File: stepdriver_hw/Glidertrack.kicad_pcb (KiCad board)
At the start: 2 copper layers, 25 parts

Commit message: HW: start to trace pcb.
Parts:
- added C15: C, CAP_0603, F.Cu at (261.6, 186.7)
- added C16: C, CAP_0603, F.Cu at (256.5, 186.7)
- added C17: C, CAP_0603, F.Cu at (265.4, 186.7)
- added D1: DIODE, DIODE_SOD323, F.Cu at (172.7, 144.8)
- added D2: LED, LED_ANGLE, F.Cu at (226.1, 186.7)
- added D3: LED, LED_ANGLE, F.Cu at (231.1, 186.7)
- added D4: LED, LED_ANGLE, F.Cu at (234.9, 186.7)
- added DA3: LD1117, SOT223, F.Cu at (154.9, 151.1)
- added F1: FUSE0R, RES_0603, F.Cu at (243.8, 186.7)
- added R6: R, RES_0603, F.Cu at (247.7, 186.7)
- added R7: R, RES_0603, F.Cu at (238.8, 186.7)
- added R8: R, RES_0603, F.Cu at (234.9, 195.6)
- added XL10: CONN_8, CONN_PLS-8, F.Cu at (152.4, 174.0)
- added XL3: CONN_3, CONN_PLS-3, F.Cu at (204.5, 170.2)
- added XL4: CONN_2, CONN_PLS-2, F.Cu at (204.5, 162.6)
- added XL5: CONN_3, CONN_PLS-3, F.Cu at (146.1, 166.4)
- added XL6: CONN_10, CONN_IDC_2X5, F.Cu at (138.4, 149.9)
- added XL7: CONN_3, CONN_PLS-3, F.Cu at (135.9, 168.9)
- added XL8: BARREL_SOCKET, CONN_BARREL, F.Cu at (152.4, 142.2)
- added XL9: CONN_8, CONN_PLS-8, F.Cu at (174.0, 174.0)
- added XTAL1: CRYSTAL, CRYSTAL_HC49, F.Cu at (181.6, 162.6)
- moved C5 290.5 mm to (265.4, 191.8)
- moved R4 288.7 mm to (256.5, 191.8)
- moved C6 284.9 mm to (261.6, 191.8)
- moved C11 279.1 mm to (234.9, 191.8)
- moved R1 274.9 mm to (252.7, 186.7)
- moved C8 273.0 mm to (252.7, 191.8)
- moved C12 272.6 mm to (229.9, 191.8)
- moved C1 272.2 mm to (226.1, 195.6)
- moved C10 267.1 mm to (226.1, 191.8)
- moved C9 266.6 mm to (247.7, 191.8)
- moved C2 265.9 mm to (221.0, 195.6)
- moved R2 265.2 mm to (229.9, 195.6)
- moved C14 261.4 mm to (243.8, 191.8)
- moved C3 260.8 mm to (217.2, 195.6)
- moved R3 258.4 mm to (221.0, 191.8)
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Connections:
- DA1 pad 4: +3.3V -> +5V
- DA1 pad 5: +5V -> +3.3V
- DD1 pad 10: (no net) -> /ENDSTOP1
- DD1 pad 11: (no net) -> /ENDSTOP2
- DD1 pad 12: (no net) -> /WIFI_TX
- DD1 pad 13: (no net) -> /WIFI_RX
- DD1 pad 14: (no net) -> /MOTOR_SPI_CS
- DD1 pad 15: (no net) -> /MOTOR_SPI_SCK
- DD1 pad 16: (no net) -> /MOTOR_SPI_MISO
- DD1 pad 17: (no net) -> /MOTOR_SPI_MOSI
- DD1 pad 18: (no net) -> /MOTOR_STBY
- DD1 pad 19: (no net) -> /MOTOR_BUSY
- DD1 pad 20: (no net) -> /MOTOR_FLAG
- DD1 pad 21: (no net) -> /GPIOB10
- DD1 pad 22: (no net) -> /GPIOB11
- DD1 pad 25: (no net) -> /GPIOB12
- DD1 pad 26: (no net) -> /GPIOB13
- DD1 pad 27: (no net) -> /GPIOB14
- DD1 pad 28: (no net) -> /GPIOB15
- DD1 pad 29: (no net) -> /MOTOR_STCK
- DD1 pad 30: (no net) -> /DEBUG_TX
- DD1 pad 31: (no net) -> /DEBUG_RX
- DD1 pad 39: (no net) -> /GPIOB3
- DD1 pad 40: (no net) -> /GPIOB4
- DD1 pad 41: (no net) -> /GPIOB5
- DD1 pad 42: (no net) -> /GPIOB6
- DD1 pad 43: (no net) -> /GPIOB7
- DD1 pad 45: (no net) -> /GPIOB8
- DD1 pad 46: (no net) -> /GPIOB9
- MDL1 pad 14: (no net) -> N-0000074
- MDL1 pad 15: (no net) -> N-0000075
- MDL1 pad 2: (no net) -> /WIFI_BOOT
- MDL1 pad 23: (no net) -> GND
- MDL1 pad 24: (no net) -> +3.3V
- MDL1 pad 3: (no net) -> /WIFI_RESET
- MDL1 pad 5: (no net) -> N-0000076
- MDL1 pad 6: (no net) -> /WIFI_RX
- MDL1 pad 8: (no net) -> /WIFI_TX
- MDL1 pad PAD: (no net) -> GND
- XL1 pad 1: +5V -> N-0000069
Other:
- board outline added: 73.7 x 44.4 mm

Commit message: HW: component placed.
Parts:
- removed D2, D3, D4: LED, LED_ANGLE
- removed XL10: CONN_8, CONN_PLS-8
- added C18: 0.1u, CAP_0603, F.Cu at (144.2, 151.7)
- added DA4: EEPROM_SPI, SO8E, F.Cu at (162.6, 156.6)
- added LINK_UP1: LED, LED_ANGLE, F.Cu at (116.8, 153.4)
- added POWER_UP1: LED, LED_ANGLE, F.Cu at (116.8, 157.6)
- added R10: 22K, RES_0603, F.Cu at (147.6, 135.9)
- added R9: 22K, RES_0603, F.Cu at (147.6, 134.3)
- added RUN1: LED, LED_ANGLE, F.Cu at (116.8, 161.8)
- C10, C9: value C -> 15p
- C15: value C -> 0.1u
- C16: value C -> 10u
- R5: value R -> 1K2
- R6, R7, R8: value R -> 22R
- XTAL1: value CRYSTAL -> 8/16 MHz
- moved R6 132.1 mm to (118.8, 157.6), turned to 90 degrees
- moved R7 124.4 mm to (118.8, 153.4), turned to 90 degrees
- moved R8 121.0 mm to (118.8, 161.8), turned to 90 degrees
- moved C9 115.2 mm to (137.9, 156.4), turned to 270 degrees
- moved R4 109.6 mm to (159.0, 141.8), turned to 90 degrees
- moved C13 101.9 mm to (147.2, 147.1), turned to 90 degrees
- moved C17 101.4 mm to (169.0, 155.2)
- moved F1 99.5 mm to (147.9, 160.2), turned to 180 degrees
- moved C5 99.3 mm to (171.8, 158.7), turned to 90 degrees
- moved C14 97.4 mm to (157.7, 146.4), turned to 90 degrees
- moved C6 97.3 mm to (170.2, 158.7), turned to 90 degrees
- moved R1 96.7 mm to (166.2, 143.5), turned to 270 degrees
- moved C15 96.6 mm to (174.9, 144.1), turned to 180 degrees
- moved C10 93.8 mm to (137.9, 159.7), turned to 90 degrees
- moved C8 92.0 mm to (169.0, 153.6)
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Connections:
- DD1 pad 21: /GPIOB10 -> /EE_WRITE
- DD1 pad 22: /GPIOB11 -> /EE_HOLD
- DD1 pad 25: /GPIOB12 -> (no net)
- DD1 pad 26: /GPIOB13 -> /EE_SCK
- DD1 pad 27: /GPIOB14 -> /EE_MISO
- DD1 pad 28: /GPIOB15 -> /EE_MOSI
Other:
- board size 73.7 x 44.4 mm -> 73.2 x 38.4 mm

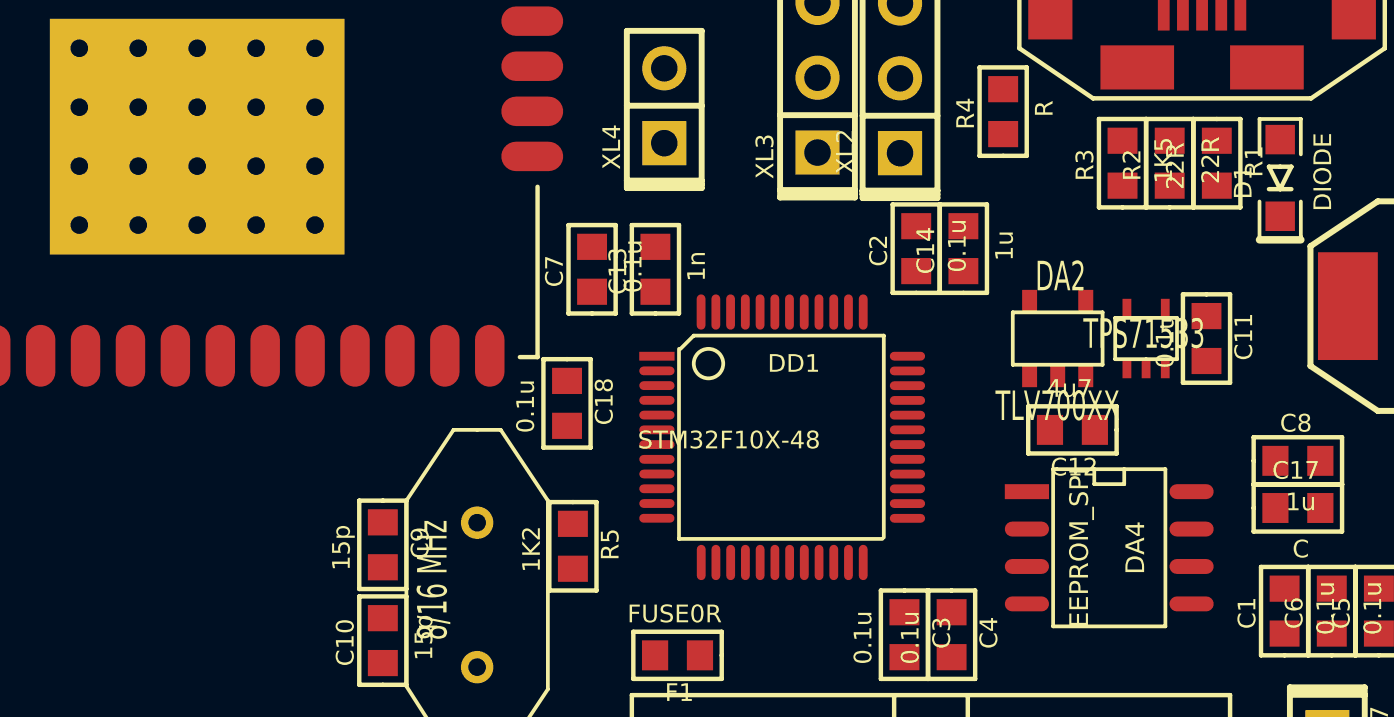
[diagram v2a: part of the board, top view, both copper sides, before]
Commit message: HW: added MOSFET transistor on power WiFi module.
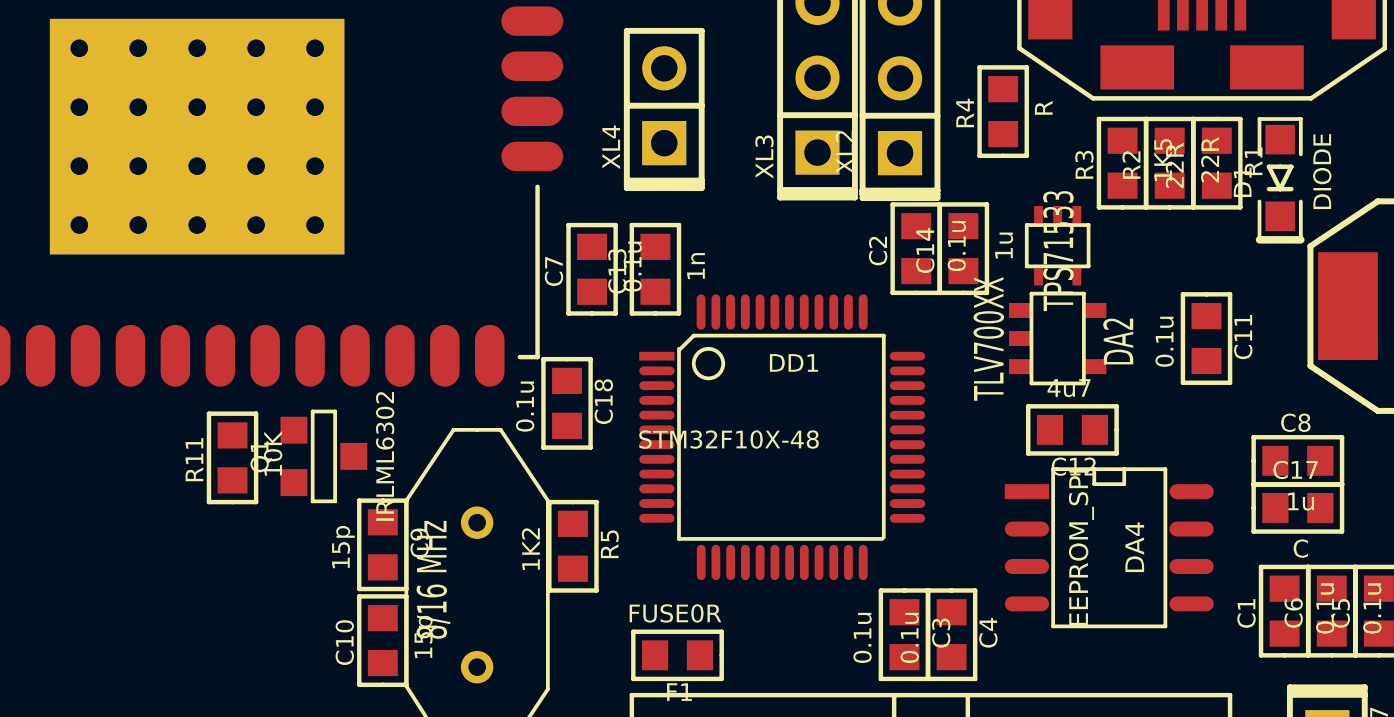
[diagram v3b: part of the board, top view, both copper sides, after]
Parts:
- added Q1: IRLML6302, SOT23, F.Cu at (135.9, 153.4)
- added R11: 10K, RES_0603, F.Cu at (132.8, 153.5)
- moved DA1 4.35 mm to (160.8, 146.3), turned to 270 degrees
- turned DA2 to 270 degrees
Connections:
- C17 pad 1: +3.3V -> N-0000083
- MDL1 pad 24: +3.3V -> N-0000083
- R10 pad 1: +3.3V -> N-0000083
- R9 pad 1: +3.3V -> N-0000083
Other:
- net class Default: clearance 0.254 -> 0.2; trace_width 0.254 -> 0.2; via_dia 0.889 -> 0.8; via_drill 0.635 -> 0.4
- net class PWR added: clearance 0.3, trace_width 0.5, via_dia 0.8, via_drill 0.4
- rule pad_to_mask_clearance: 0 -> 0.2
- rule trace_clearance: 0.254 -> 0.2
- rule trace_min: 0.254 -> 0.2
- rule via_min_drill: 0.508 -> 0.3
- rule via_min_size: 0.889 -> 0.7

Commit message: HW: PCB design proceed.
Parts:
- added HOLE1: HOLE_METALLED, Hole3_5_out6mm, F.Cu at (319.2, 93.8)
- added HOLE2: HOLE_METALLED, Hole3_5_out6mm, F.Cu at (274.0, 100.9)
- moved XL9 169.2 mm to (279.0, 78.7)
- moved R4 163.7 mm to (310.5, 79.7), turned to 0 degrees
- moved RUN1 163.0 mm to (257.1, 78.9), turned to 180 degrees
- moved F1 162.9 mm to (297.5, 95.5)
- moved XL1 161.1 mm to (317.4, 83.2), turned to 180 degrees
- moved C13 160.9 mm to (296.2, 86.5), turned to 270 degrees
- moved R3 160.0 mm to (310.5, 81.3), turned to 0 degrees
- moved XL7 159.4 mm to (303.8, 78.7), turned to 180 degrees
- moved R8 158.7 mm to (254.1, 78.9), turned to 180 degrees
- moved R2 157.9 mm to (310.5, 82.9), turned to 0 degrees
- moved C3 156.4 mm to (292.5, 83.7), turned to 90 degrees
- moved R1 155.8 mm to (310.5, 84.5), turned to 180 degrees
- moved XL6 154.9 mm to (297.7, 102.1), turned to 0 degrees
- moved C12 154.7 mm to (301.4, 86.8), turned to 90 degrees
- moved C14 154.3 mm to (298.9, 84.4), turned to 180 degrees
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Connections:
- C17 pad 1: N-0000083 -> N-0000081
- DD1 pad 39: /GPIOB3 -> /WIFI_PWR
- MDL1 pad 24: N-0000083 -> N-0000081
- Q1 pad 3: N-0000083 -> N-0000081
- R10 pad 1: N-0000083 -> +3.3V
- R9 pad 1: N-0000083 -> +3.3V
- XL9 pad 8: /GPIOB3 -> +3.3V
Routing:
- net GND: track 0.00 -> 73.3 mm
- net +3.3V: track 0.00 -> 54.3 mm, vias 0 -> 4
- net +5V: track 0.00 -> 29.7 mm
- net /USB_DM: track 0.00 -> 22.5 mm
- net /USB_DP: track 0.00 -> 22.5 mm
- net /WIFI_TX: track 0.00 -> 21.4 mm
- net /WIFI_RX: track 0.00 -> 18.1 mm
- net /WIFI_RESET: track 0.00 -> 15.4 mm
- net /WIFI_BOOT: track 0.00 -> 13.0 mm
- net +12V: track 0.00 -> 11.3 mm
- net N-0000080: track 0.00 -> 10.8 mm
- net N-000003: track 0.00 -> 9.88 mm
- net N-0000069: track 0.00 -> 8.32 mm
- net N-0000077: track 0.00 -> 7.19 mm
- net N-0000082: track 0.00 -> 6.88 mm
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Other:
- board size 73.2 x 38.4 mm -> 84 x 30 mm

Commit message: HW: PCB design complete.
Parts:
- moved R9 16.4 mm to (271.8, 97.5), turned to 90 degrees
- moved XL4 15.8 mm to (264.7, 81.7), turned to 180 degrees
- moved R10 14.5 mm to (273.4, 97.5), turned to 90 degrees
- moved R11 7.02 mm to (269.2, 97.5), turned to 90 degrees
- moved C1 5.63 mm to (296.0, 90.7), turned to 90 degrees
- moved C2 5.63 mm to (294.4, 90.7), turned to 90 degrees
- moved C17 4.28 mm to (264.5, 102.0)
- moved F1 3.30 mm to (300.8, 95.5), turned to 90 degrees
- moved Q1 3.28 mm to (268.0, 102.0)
- moved HOLE2 2.12 mm to (273.7, 103.0)
- moved C13 1.46 mm to (296.6, 85.1)
- moved C5 1.30 mm to (280.3, 83.0)
- moved C6 1.30 mm to (281.9, 83.0)
- moved R5 0.80 mm to (278.1, 90.4)
- moved C12 0.20 mm to (301.6, 86.8)
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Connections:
- net N-0000081 renamed /PWR
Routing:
- net GND: track 73.3 -> 337.0 mm, vias 0 -> 14
- net +3.3V: track 54.3 -> 153.7 mm, vias 4 -> 10
- net /WIFI_PWR: track 0.00 -> 35.1 mm, vias 0 -> 2
- net /ENDSTOP2: track 0.00 -> 30.7 mm
- net /USB_CABLE: track 0.00 -> 30.3 mm, vias 0 -> 2
- net /ENDSTOP1: track 0.00 -> 29.5 mm, vias 0 -> 1
- net /MOTOR_SPI_SCK: track 0.00 -> 29.4 mm, vias 0 -> 1
- net /MOTOR_STBY: track 0.00 -> 29.2 mm, vias 0 -> 1
- net /MOTOR_SPI_CS: track 0.00 -> 26.6 mm, vias 0 -> 1
- net /MOTOR_SPI_MOSI: track 0.00 -> 24.6 mm, vias 0 -> 1
- net /MOTOR_SPI_MISO: track 0.00 -> 22.3 mm, vias 0 -> 1
- net /DEBUG_RX: track 0.00 -> 22.3 mm, vias 0 -> 1
- net /DEBUG_TX: track 0.00 -> 22.2 mm, vias 0 -> 1
- net /MOTOR_STCK: track 0.00 -> 22.0 mm, vias 0 -> 1
- net /MOTOR_BUSY: track 0.00 -> 21.1 mm, vias 0 -> 1
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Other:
- board text added: "Glidertrack v.1.0"

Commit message: HW: add gerber files.
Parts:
- moved XTAL1 0.58 mm to (274.9, 89.6)
- moved C10 0.51 mm to (271.7, 87.9)
- moved C9 0.24 mm to (271.7, 91.4)
- moved R5 0.12 mm to (278.1, 90.3)
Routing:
- net GND: track 337.0 -> 369.5 mm, vias 14 -> 37
- net +3.3V: track 153.7 -> 126.9 mm
- net /WIFI_TX: track 41.2 -> 33.4 mm
- net /MOTOR_FLAG: track 18.8 -> 13.7 mm
- net /EE_WRITE: track 16.0 -> 11.6 mm
- net /EE_HOLD: track 12.3 -> 7.79 mm
- net /USB_CABLE: track 30.3 -> 26.0 mm
- net /MOTOR_SPI_MOSI: track 24.6 -> 20.3 mm
- net /DEBUG_TX: track 22.2 -> 18.3 mm
- net +12V: track 15.1 -> 11.2 mm
- net /MOTOR_BUSY: track 21.1 -> 17.3 mm
- net /MOTOR_SPI_CS: track 26.6 -> 22.8 mm
- net /SWDIO: track 14.7 -> 11.0 mm
- net /MOTOR_STCK: track 22.0 -> 18.3 mm
- net /MOTOR_STBY: track 29.2 -> 25.4 mm
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- added copper zone on B.Cu, net GND
- added copper zone on F.Cu, net GND
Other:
- rule pad_to_mask_clearance: 0.2 -> 0.1
- rule solder_mask_min_width: 0.2 -> 0.1
